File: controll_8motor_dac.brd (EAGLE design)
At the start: 119.4 x 73.3 mm, 61 parts

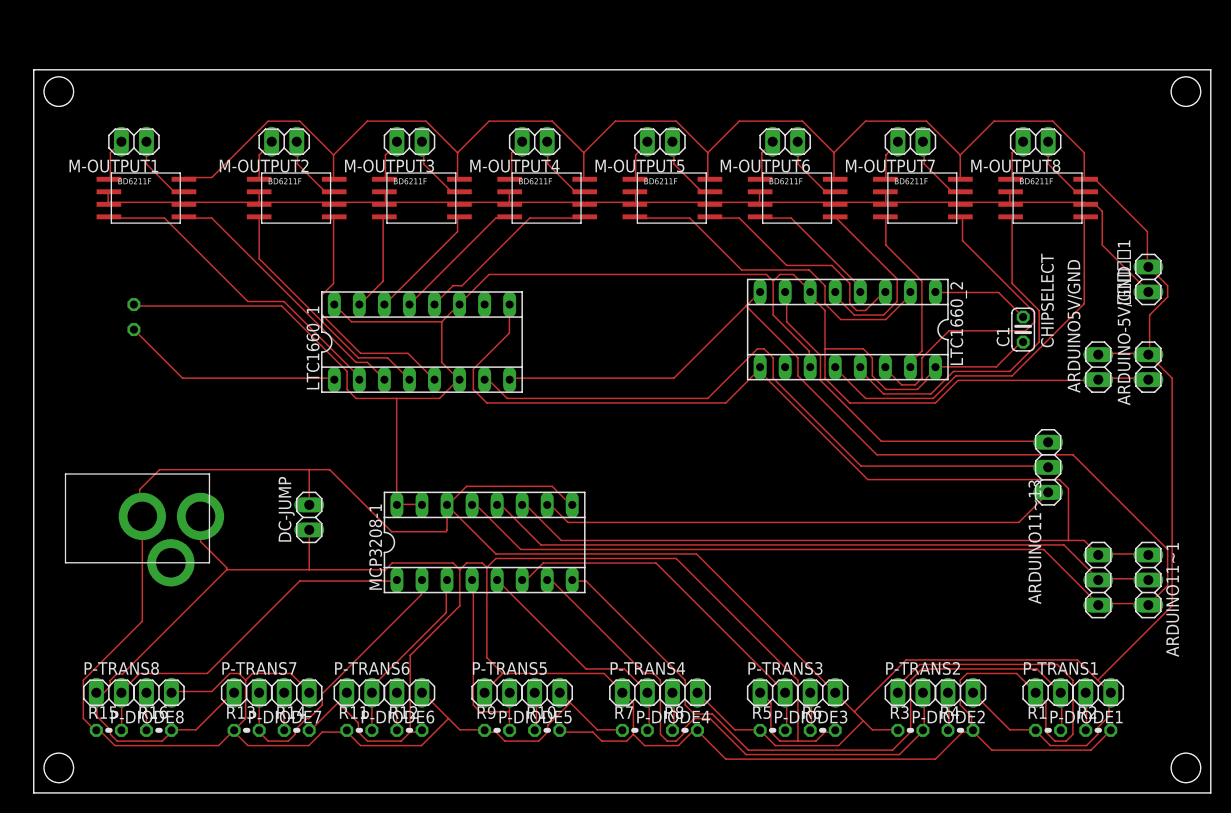
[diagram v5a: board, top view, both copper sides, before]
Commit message: 変換基盤を乗せるバージョン．(まだ微妙に刺さらない) - モータドライバ壊れた時ように変換基盤付けたほうがよいよというアドバイスを受けて
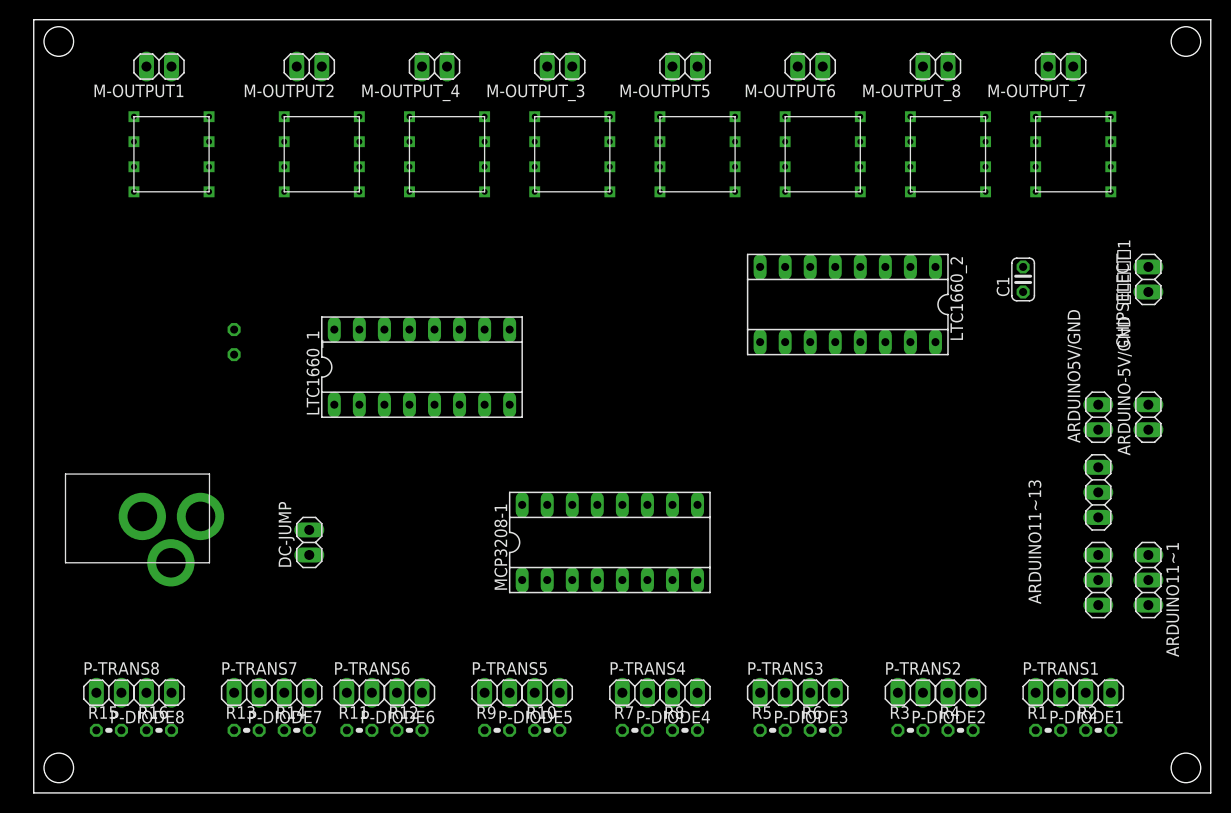
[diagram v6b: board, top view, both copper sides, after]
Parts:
- removed M-DRIVER_1, M-DRIVER_2, M-DRIVER_3, M-DRIVER_4, M-DRIVER_5, M-DRIVER_6, M-DRIVER_7, M-DRIVER_8: BD6211F-E2, BD6211F:BD6211F-E2
- removed M-OUTPUT3, M-OUTPUT4, M-OUTPUT7, M-OUTPUT8: (no value), pinhead:1X02
- added M-DRIVER1, M-DRIVER2, M-DRIVER3, M-DRIVER4, M-DRIVER5, M-DRIVER6, M-DRIVER7, M-DRIVER8: SOP8-DIP-CONVERTER, SOP8-DIP-Converter:SOP8-DIP-CONVERTER
- added M-OUTPUT_3, M-OUTPUT_4, M-OUTPUT_7, M-OUTPUT_8: (no value), pinhead:1X02
- moved MCP3208‐1 12.7 mm to (58.4, 25.4)
- moved C2 10.5 mm to (20.3, 45.7)
- moved M-OUTPUT5 8.03 mm to (66.0, 73.7)
- moved M-OUTPUT2 8.03 mm to (27.9, 73.7)
- moved M-OUTPUT1 8.03 mm to (12.7, 73.7)
- moved M-OUTPUT6 8.03 mm to (78.7, 73.7)
- moved CHIPSELECT 5.68 mm to (108.0, 30.5)
- moved ARDUINO-5V/GND 5.08 mm to (113.0, 38.1)
- moved ARDUINO5V/GND 5.08 mm to (108.0, 38.1)
- moved C1 5.08 mm to (100.3, 52.1)
- moved DC-JUMP 2.54 mm to (27.9, 25.4)
- moved LTC1660_1 2.54 mm to (39.4, 43.2)
- moved LTC1660_2 2.54 mm to (82.5, 49.5)
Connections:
- net N$1: now also M-DRIVER3.5; no longer M-DRIVER_4.5
- net N$10: now also M-DRIVER2.4; no longer M-DRIVER_2.4
- net N$11: now also M-DRIVER1.5; no longer M-DRIVER_1.5
- net N$12: now also M-DRIVER1.4; no longer M-DRIVER_1.4
- net N$13: now also M-DRIVER5.１; no longer M-DRIVER_5.1
- net N$14: now also M-DRIVER6.4; no longer M-DRIVER_6.4
- net N$15: now also M-DRIVER5.5; no longer M-DRIVER_5.5
- net N$16: now also M-DRIVER5.4; no longer M-DRIVER_5.4
- net N$17: now also M-DRIVER3.7, M-OUTPUT_3.1; no longer M-DRIVER_4.7, M-OUTPUT4.1
- net N$18: now also M-DRIVER4.7, M-OUTPUT_4.1; no longer M-DRIVER_3.7, M-OUTPUT3.1
- net N$19: now also M-DRIVER4.１, M-OUTPUT_4.2; no longer M-DRIVER_3.1, M-OUTPUT3.2
- net N$2: now also M-DRIVER3.１, M-OUTPUT_3.2; no longer M-DRIVER_4.1, M-OUTPUT4.2
- net N$20: now also M-DRIVER7.7, M-OUTPUT_7.1; no longer M-DRIVER_8.7, M-OUTPUT8.1
- net N$21: now also M-DRIVER7.１, M-OUTPUT_7.2; no longer M-DRIVER_8.1, M-OUTPUT8.2
- net N$22: now also M-DRIVER8.7, M-OUTPUT_8.1; no longer M-DRIVER_7.7, M-OUTPUT7.1
- net N$23: now also M-DRIVER8.１, M-OUTPUT_8.2; no longer M-DRIVER_7.1, M-OUTPUT7.2
- net N$24: now also M-DRIVER1.7; no longer M-DRIVER_1.7
- net N$26: now also M-DRIVER4.5; no longer M-DRIVER_3.5
- net N$27: now also M-DRIVER2.7; no longer M-DRIVER_2.7
- net N$28: now also M-DRIVER2.１; no longer M-DRIVER_2.1
- net N$29: now also M-DRIVER6.5; no longer M-DRIVER_6.5
- net N$3: now also M-DRIVER3.4; no longer M-DRIVER_4.4
- net N$30: now also M-DRIVER5.7; no longer M-DRIVER_5.7
- net N$31: now also M-DRIVER6.１; no longer M-DRIVER_6.1
- net N$32: now also M-DRIVER6.7; no longer M-DRIVER_6.7
- net N$33: now also M-DRIVER1.2, M-DRIVER1.3, M-DRIVER1.6, M-DRIVER2.2, M-DRIVER2.3, M-DRIVER2.6, M-DRIVER3.2, M-DRIVER3.3, M-DRIVER3.6, M-DRIVER4.2, M-DRIVER4.3, M-DRIVER4.6, M-DRIVER5.2, M-DRIVER5.3, M-DRIVER5.6, M-DRIVER6.2, M-DRIVER6.3, M-DRIVER6.6, M-DRIVER7.2, M-DRIVER7.3, M-DRIVER7.6, M-DRIVER8.2, M-DRIVER8.3, M-DRIVER8.6; no longer M-DRIVER_1.2, M-DRIVER_1.3, M-DRIVER_1.6, M-DRIVER_2.2, M-DRIVER_2.3, M-DRIVER_2.6, M-DRIVER_3.2, M-DRIVER_3.3, M-DRIVER_3.6, M-DRIVER_4.2, M-DRIVER_4.3, M-DRIVER_4.6, M-DRIVER_5.2, M-DRIVER_5.3, M-DRIVER_5.6, M-DRIVER_6.2, M-DRIVER_6.3, M-DRIVER_6.6, M-DRIVER_7.2, M-DRIVER_7.3, M-DRIVER_7.6, M-DRIVER_8.2, M-DRIVER_8.3, M-DRIVER_8.6
- net N$4: now also M-DRIVER4.4; no longer M-DRIVER_3.4
- net N$40: now also M-DRIVER1.１; no longer M-DRIVER_1.1
- net N$5: now also M-DRIVER7.5; no longer M-DRIVER_8.5
- net N$6: now also M-DRIVER7.4; no longer M-DRIVER_8.4
- net N$7: now also M-DRIVER8.5; no longer M-DRIVER_7.5
- net N$8: now also M-DRIVER8.4; no longer M-DRIVER_7.4
- net N$9: now also M-DRIVER2.5; no longer M-DRIVER_2.5
- net P-DIORD1: now also M-DRIVER1.8, M-DRIVER2.8, M-DRIVER3.8, M-DRIVER4.8, M-DRIVER5.8, M-DRIVER6.8, M-DRIVER7.8, M-DRIVER8.8; no longer M-DRIVER_1.8, M-DRIVER_2.8, M-DRIVER_3.8, M-DRIVER_4.8, M-DRIVER_5.8, M-DRIVER_6.8, M-DRIVER_7.8, M-DRIVER_8.8
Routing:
- net P-DIORD1: track 491.9 -> 0.00 mm
- net N$97: track 309.4 -> 0.00 mm
- net ARDUINO-5V/GND: track 190.9 -> 0.00 mm
- net N$38: track 162.5 -> 0.00 mm
- net N$25: track 149.0 -> 0.00 mm
- net N$33: track 123.6 -> 0.00 mm
- net N$53: track 69.6 -> 0.00 mm
- net N$42: track 69.4 -> 0.00 mm
- net N$39: track 66.3 -> 0.00 mm
- net N$52: track 55.8 -> 0.00 mm
- net N$44: track 52.9 -> 0.00 mm
- net N$5: track 39.5 -> 0.00 mm
- net N$54: track 36.9 -> 0.00 mm
- net N$59: track 36.6 -> 0.00 mm
- net N$41: track 36.2 -> 0.00 mm
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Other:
- board size 119.4 x 73.3 mm -> 119.4 x 78.4 mm

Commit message: 配線してみた,icパーツ使ってみた
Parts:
- M-DRIVER1, M-DRIVER2, M-DRIVER3, M-DRIVER4, M-DRIVER5, M-DRIVER6, M-DRIVER7, M-DRIVER8: value SOP8-DIP-CONVERTER -> (none); device SOP8-DIP-Converter:SOP8-DIP-CONVERTER -> ic-package:SOCKET-08
- moved M-DRIVER3 12.7 mm to (40.6, 63.5), turned to 270 degrees
- moved M-DRIVER4 12.7 mm to (53.3, 63.5), turned to 270 degrees
- moved M-DRIVER7 12.7 mm to (91.4, 63.5), turned to 270 degrees
- moved M-DRIVER8 12.7 mm to (104.1, 63.5), turned to 270 degrees
- moved M-OUTPUT_3 12.7 mm to (40.6, 73.7)
- moved M-OUTPUT_4 12.7 mm to (53.3, 73.7)
- moved M-OUTPUT_7 12.7 mm to (91.4, 73.7)
- moved M-OUTPUT_8 12.7 mm to (104.1, 73.7)
- moved P-TRANS4 5.08 mm to (66.0, 10.2)
- moved R7 5.08 mm to (66.0, 6.35)
- moved P-DIODE3 5.08 mm to (85.1, 10.2)
- moved P-DIODE4 5.08 mm to (71.1, 10.2)
- moved P-DIODE5 5.08 mm to (57.1, 10.2)
- moved P-DIODE6 5.08 mm to (43.2, 10.2)
- moved P-TRANS3 5.08 mm to (80.0, 10.2)
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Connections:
- net N$13: now also M-DRIVER5.1; no longer M-DRIVER5.１
- net N$19: now also M-DRIVER4.1; no longer M-DRIVER4.１
- net N$2: now also M-DRIVER3.1; no longer M-DRIVER3.１
- net N$21: now also M-DRIVER7.1; no longer M-DRIVER7.１
- net N$23: now also M-DRIVER8.1; no longer M-DRIVER8.１
- net N$28: now also M-DRIVER2.1; no longer M-DRIVER2.１
- net N$31: now also M-DRIVER6.1; no longer M-DRIVER6.１
- net N$40: now also M-DRIVER1.1; no longer M-DRIVER1.１
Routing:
- net P-DIORD1: track 0.00 -> 608.3 mm
- net N$97: track 0.00 -> 244.3 mm
- net ARDUINO-5V/GND: track 0.00 -> 238.5 mm
- net N$38: track 0.00 -> 164.3 mm
- net N$25: track 0.00 -> 161.1 mm
- net N$33: track 0.00 -> 135.2 mm
- net N$52: track 0.00 -> 93.2 mm
- net N$42: track 0.00 -> 68.5 mm
- net N$39: track 0.00 -> 65.9 mm
- net N$44: track 0.00 -> 62.0 mm
- net N$53: track 0.00 -> 59.5 mm
- net N$59: track 0.00 -> 46.8 mm
- net N$41: track 0.00 -> 46.0 mm
- net N$16: track 0.00 -> 37.7 mm
- net N$58: track 0.00 -> 35.7 mm
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
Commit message: 配線しなおし
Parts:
- moved ARDUINO11~1 5.08 mm to (113.0, 26.7)
- moved ARDUINO11~13 5.08 mm to (108.0, 26.7)
- moved CHIPSELECT 5.08 mm to (108.0, 35.6)
- moved ARDUINO-5V/GND 5.08 mm to (113.0, 43.2)
- moved ARDUINO5V/GND 5.08 mm to (108.0, 43.2)
- moved LTC1660_2 5.08 mm to (77.5, 47.0)
- moved MCP3208‐1 3.59 mm to (61.0, 22.9)
- moved LTC1660_1 2.54 mm to (41.9, 43.2)
- moved 安定化電源1 2.54 mm to (113.0, 52.1)
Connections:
- removed net N$34: C2.2, LTC1660_1.1
- removed net N$35: C1.2, LTC1660_2.1
- removed net P-DIORD1: ARDUINO-5V/GND.2, ARDUINO5V/GND.2, DC-JUMP.2, M-DRIVER1.8, M-DRIVER2.8, M-DRIVER3.8, M-DRIVER4.8, M-DRIVER5.8, M-DRIVER6.8, M-DRIVER7.8, M-DRIVER8.8, MCP3208‐1.14, MCP3208‐1.9, P-DIODE1.1, P-DIODE2.1, P-DIODE3.1, P-DIODE4.1, P-DIODE5.1, P-DIODE6.1, P-DIODE7.1, P-DIODE8.1, R1.1, R11.1, R13.1, R15.1, R3.1, R5.1, R7.1, R9.1, U$1.RING, 安定化電源1.2
- new net GND: ARDUINO-5V/GND.2, ARDUINO5V/GND.2, C1.2, C2.2, DC-JUMP.2, LTC1660_1.1, LTC1660_2.1, M-DRIVER1.8, M-DRIVER2.8, M-DRIVER3.8, M-DRIVER4.8, M-DRIVER5.8, M-DRIVER6.8, M-DRIVER7.8, M-DRIVER8.8, MCP3208‐1.14, MCP3208‐1.9, P-DIODE1.1, P-DIODE2.1, P-DIODE3.1, P-DIODE4.1, P-DIODE5.1, P-DIODE6.1, P-DIODE7.1, P-DIODE8.1, R1.1, R11.1, R13.1, R15.1, R3.1, R5.1, R7.1, R9.1, U$1.RING, 安定化電源1.2
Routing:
- net GND: track 0.00 -> 678.1 mm
- net P-DIORD1: track 608.3 -> 0.00 mm
- net N$25: track 161.1 -> 57.9 mm
- net N$52: track 93.2 -> 34.0 mm
- net N$97: track 244.3 -> 197.8 mm
- net N$38: track 164.3 -> 142.2 mm
- net N$53: track 59.5 -> 42.1 mm
- net N$44: track 62.0 -> 44.8 mm
- net N$7: track 31.8 -> 47.4 mm
- net N$42: track 68.5 -> 53.3 mm
- net N$34: track 14.8 -> 0.00 mm
- net ARDUINO-5V/GND: track 238.5 -> 228.7 mm
- net N$35: track 6.51 -> 0.00 mm
- net N$54: track 30.0 -> 24.1 mm
- net N$59: track 46.8 -> 51.4 mm
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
